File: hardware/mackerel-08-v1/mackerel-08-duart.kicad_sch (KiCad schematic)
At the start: 18 parts, among them J2 Conn_01x06, J3 Conn_01x06, J5 Conn_02x04_Odd_Even, J6 Conn_02x04_Odd_Even, J7 Conn_02x04_Odd_Even, U15 XR68C681, X2 CXO_DIP8

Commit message: Fixed most of the problems with rev 1
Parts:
- removed J5, J6, J7: Conn_02x04_Odd_Even, Connector_IDC:IDC-Header_2x04_P2.54mm_Vertical, symbol Connector_Generic:Conn_02x04_Odd_Even
- removed X2: CXO_DIP8, Oscillator:Oscillator_DIP-8, symbol Oscillator:CXO_DIP8
- added J8: Conn_01x08, Connector_PinSocket_2.54mm:PinSocket_1x08_P2.54mm_Vertical, symbol Connector_Generic:Conn_01x08
- added X2: CXO_DIP14, Oscillator:Oscillator_DIP-14, symbol Oscillator:CXO_DIP14
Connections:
- net +5V: now also X2.14 (Vcc)
- net GND: now also X2.7 (GND)
- net USR_LED: now reaches R13.1, U15.17 (OP7)
- net at U15.36 (X1/CLK): now also X2.8 (OUT)
- net SPI_CS0 renamed SPI_CS
- net SPI_CS1 renamed SD_CS
- net SPI_CS2 renamed X_OUT
- net SPI_INT0 renamed SPI_INT
- net SPI_INT1 renamed SD_CD
- no-connect marks 5 -> 4
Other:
- note added: "SD Header"
- note added: "TODO: SD card pinout"
- note removed: "No int on SPI2"
- note removed: "SPI Headers"

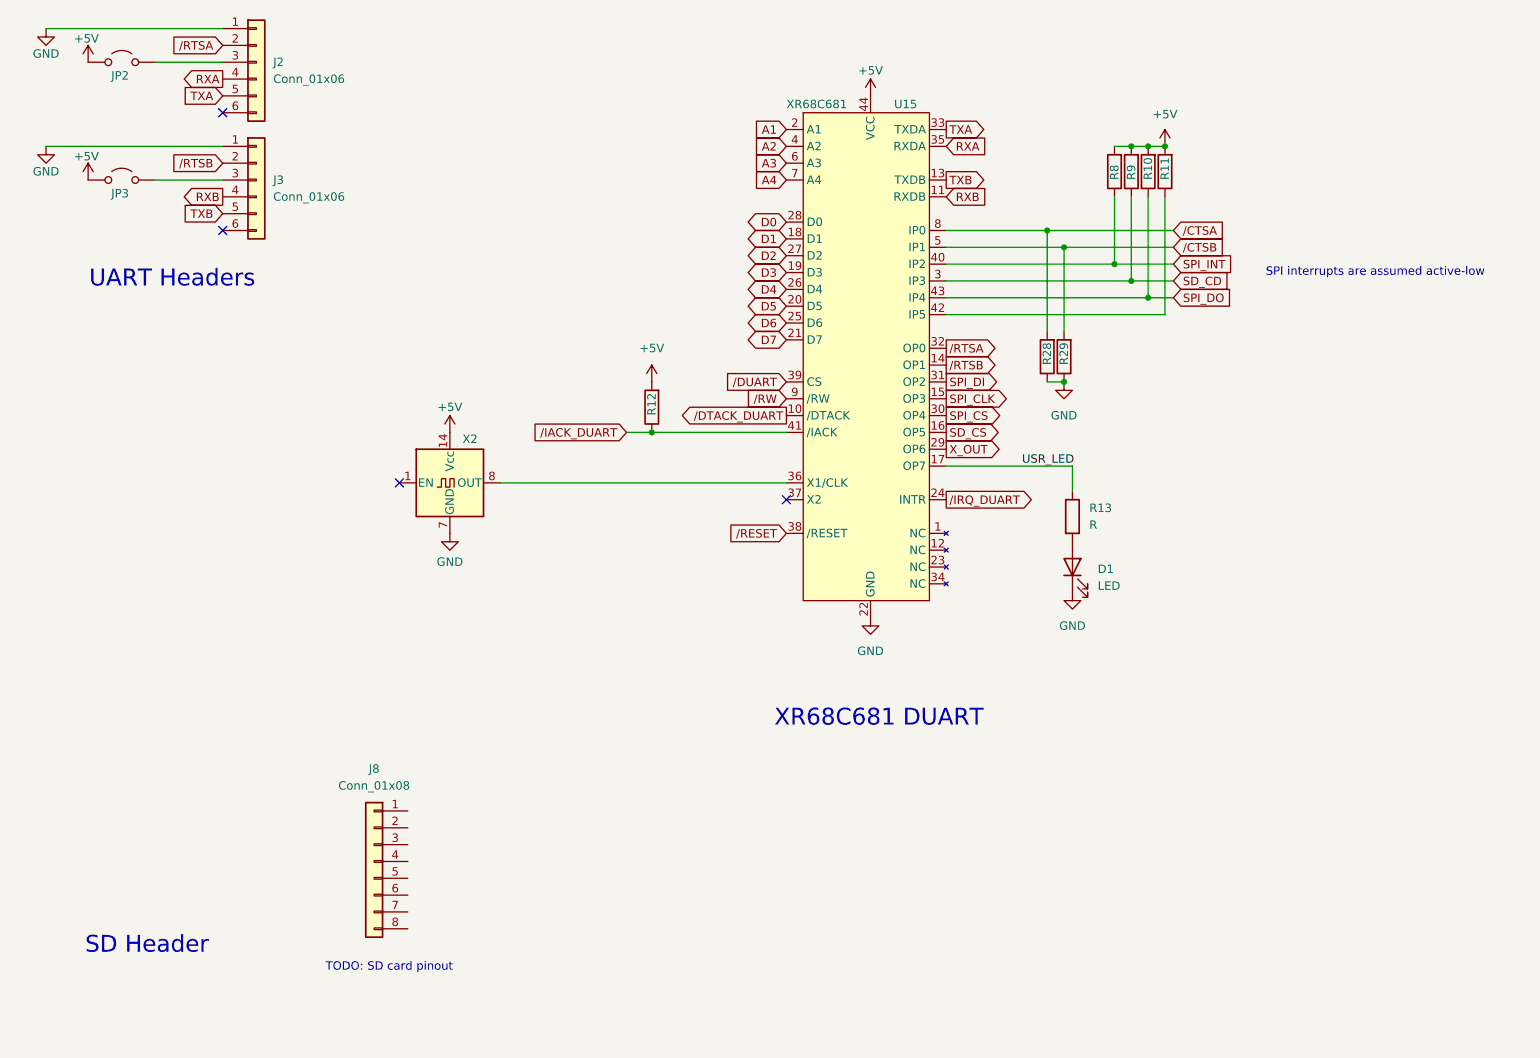
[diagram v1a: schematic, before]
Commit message: Mack-08 1.1 schematic fixes done, needs final routing
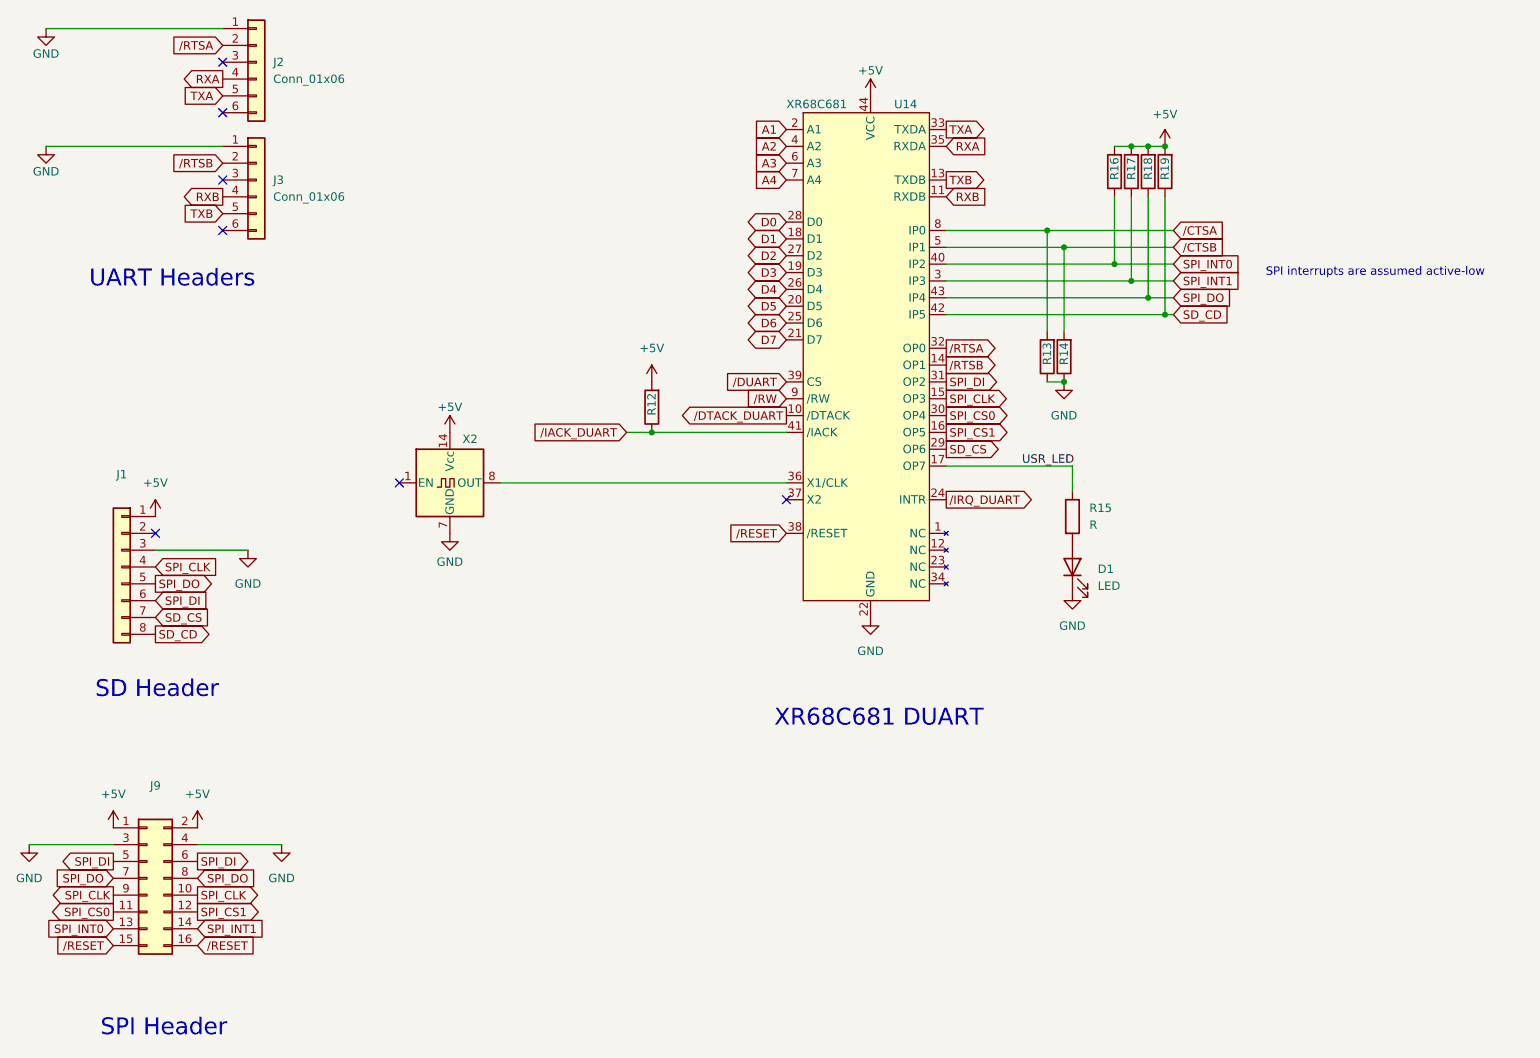
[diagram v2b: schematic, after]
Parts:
- removed J8: Conn_01x08, Connector_PinSocket_2.54mm:PinSocket_1x08_P2.54mm_Vertical, symbol Connector_Generic:Conn_01x08
- removed JP2, JP3: Jumper_2_Open, Connector_PinHeader_2.54mm:PinHeader_1x02_P2.54mm_Vertical, symbol Jumper:Jumper_2_Open
- added J1: Conn_01x08, Connector_PinSocket_2.54mm:PinSocket_1x08_P2.54mm_Vertical, symbol Connector_Generic:Conn_01x08
- added J9: Conn_02x08_Odd_Even, Connector_PinHeader_2.54mm:PinHeader_2x08_P2.54mm_Vertical, symbol Connector_Generic:Conn_02x08_Odd_Even
- renumbered R28 to R13, R29 to R14, R13 to R15, R8 to R16, R9 to R17, R10 to R18, R11 to R19, U15 to U14
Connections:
- net X_OUT is gone; now on net SD_CS: U14.29 (OP6)
- net +5V: now also J1.1 (Pin_1), J9.1 (Pin_1), J9.2 (Pin_2)
- net GND: now also J1.3 (Pin_3), J9.3 (Pin_3), J9.4 (Pin_4)
- net SD_CD: now also R19.1, U14.42 (IP5), J1.8 (Pin_8); no longer R17.1, U14.3 (IP3)
- net SD_CS: now also J1.7 (Pin_7); no longer U14.16 (OP5)
- net SPI_CLK: now also J1.4 (Pin_4), J9.10 (Pin_10), J9.9 (Pin_9)
- net SPI_DI: now also J1.6 (Pin_6), J9.5 (Pin_5), J9.6 (Pin_6)
- net SPI_DO: now also J1.5 (Pin_5), J9.7 (Pin_7), J9.8 (Pin_8)
- net /RESET: now also J9.15 (Pin_15), J9.16 (Pin_16)
- net SPI_CS renamed SPI_CS0
- net SPI_CS0: now also J9.11 (Pin_11)
- net SPI_INT renamed SPI_INT0
- net SPI_INT0: now also J9.13 (Pin_13)
- new net SPI_CS1: J9.12 (Pin_12), U14.16 (OP5)
- new net SPI_INT1: J9.14 (Pin_14), R17.1, U14.3 (IP3)
- no-connect marks 4 -> 7
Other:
- note added: "SPI Header"
- note removed: "TODO: SD card pinout"

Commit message: Mack-08 rev 1.1 routed
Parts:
- R12, R13, R14, R15, R16, R17, R18, R19: footprint Resistor_THT:R_Axial_DIN0207_L6.3mm_D2.5mm_P7.62mm_Horizontal -> Resistor_SMD:R_1206_3216Metric_Pad1.30x1.75mm_HandSolder
- renumbered J9 to J2, J2 to J3, J3 to J4
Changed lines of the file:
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@@
 			)
 		)
-		(property "Footprint" "Resistor_THT:R_Axial_DIN0207_L6.3mm_D2.5mm_P7.62mm_Horizontal"
+		(property "Footprint" "Resistor_SMD:R_1206_3216Metric_Pad1.30x1.75mm_HandSolder"
 			(at 119.888 80.01 90)
 			(effects
@@
 		(dnp no)
 		(fields_autoplaced yes)
-		(property "Reference" "#PWR044"
+		(property "Reference" "#PWR046"
 			(at 151.13 118.11 0)
 			(effects
@@
 			(project "mackerel-08-v1"
 				(path "/d8b1bce0-db11-4fa6-8e54-fcae9a8fcfc2/377dc58c-bf3b-4b5b-9c36-5a4dfaf86cf7"
-					(reference "#PWR044")
+					(reference "#PWR046")
 					(unit 1)
 				)
@@
 		(dnp no)
 		(fields_autoplaced yes)
-		(property "Reference" "#PWR045"
+		(property "Reference" "#PWR047"
 			(at 180.34 82.55 0)
 			(effects
@@
 			(project ""
 				(path "/d8b1bce0-db11-4fa6-8e54-fcae9a8fcfc2/377dc58c-bf3b-4b5b-9c36-5a4dfaf86cf7"
-					(reference "#PWR045")
+					(reference "#PWR047")
 					(unit 1)
 				)
@@
 			)
 		)
-		(property "Footprint" "Resistor_THT:R_Axial_DIN0207_L6.3mm_D2.5mm_P7.62mm_Horizontal"
+		(property "Footprint" "Resistor_SMD:R_1206_3216Metric_Pad1.30x1.75mm_HandSolder"
 			(at 192.278 44.45 90)
 			(effects
@@
 		(dnp no)
 		(fields_autoplaced yes)
-		(property "Reference" "#PWR075"
+		(property "Reference" "#PWR034"
 			(at 24.13 152.4 0)
 			(effects
@@
 			(project "mackerel-08-v1"
 				(path "/d8b1bce0-db11-4fa6-8e54-fcae9a8fcfc2/377dc58c-bf3b-4b5b-9c36-5a4dfaf86cf7"
-					(reference "#PWR075")
+					(reference "#PWR034")
 					(unit 1)
 				)
@@
 			)
 		)
-		(property "Footprint" "Resistor_THT:R_Axial_DIN0207_L6.3mm_D2.5mm_P7.62mm_Horizontal"
+		(property "Footprint" "Resistor_SMD:R_1206_3216Metric_Pad1.30x1.75mm_HandSolder"
 			(at 194.818 44.45 90)
 			(effects
@@
 		(dnp no)
 		(fields_autoplaced yes)
-		(property "Reference" "J3"
+		(property "Reference" "J4"
 			(at 60.96 45.7199 0)
 			(effects
@@
 			(project "mackerel-08-v1"
 				(path "/d8b1bce0-db11-4fa6-8e54-fcae9a8fcfc2/377dc58c-bf3b-4b5b-9c36-5a4dfaf86cf7"
-					(reference "J3")
+					(reference "J4")
 					(unit 1)
 				)
@@
 		(on_board yes)
 		(dnp no)
-		(property "Reference" "#PWR043"
+		(property "Reference" "#PWR045"
 			(at 151.13 36.83 0)
 			(effects
@@
 			(project "mackerel-08-v1"
 				(path "/d8b1bce0-db11-4fa6-8e54-fcae9a8fcfc2/377dc58c-bf3b-4b5b-9c36-5a4dfaf86cf7"
-					(reference "#PWR043")
+					(reference "#PWR045")
 					(unit 1)
 				)
@@
 		(dnp no)
 		(fields_autoplaced yes)
-		(property "Reference" "J9"
+		(property "Reference" "J2"
 			(at 43.18 137.16 0)
 			(effects
@@
 			(project ""
 				(path "/d8b1bce0-db11-4fa6-8e54-fcae9a8fcfc2/377dc58c-bf3b-4b5b-9c36-5a4dfaf86cf7"
-					(reference "J9")
+					(reference "J2")
 					(unit 1)
 				)
@@
 		(dnp no)
 		(fields_autoplaced yes)
-		(property "Reference" "#PWR046"
+		(property "Reference" "#PWR048"
 			(at 181.61 114.3 0)
 			(effects
@@
 			(project "mackerel-08-v1"
 				(path "/d8b1bce0-db11-4fa6-8e54-fcae9a8fcfc2/377dc58c-bf3b-4b5b-9c36-5a4dfaf86cf7"
-					(reference "#PWR046")
+					(reference "#PWR048")
 					(unit 1)
 				)
@@
 			)
 		)
-		(property "Footprint" "Resistor_THT:R_Axial_DIN0207_L6.3mm_D2.5mm_P7.62mm_Horizontal"
+		(property "Footprint" "Resistor_SMD:R_1206_3216Metric_Pad1.30x1.75mm_HandSolder"
 			(at 179.578 72.39 90)
 			(effects
@@
 		(dnp no)
 		(fields_autoplaced yes)
-		(property "Reference" "#PWR076"
+		(property "Reference" "#PWR041"
 			(at 62.23 152.4 0)
 			(effects
@@
 			(project "mackerel-08-v1"
 				(path "/d8b1bce0-db11-4fa6-8e54-fcae9a8fcfc2/377dc58c-bf3b-4b5b-9c36-5a4dfaf86cf7"
-					(reference "#PWR076")
+					(reference "#PWR041")
 					(unit 1)
 				)
@@
 		(on_board yes)
 		(dnp no)
-		(property "Reference" "#PWR041"
+		(property "Reference" "#PWR043"
 			(at 87.63 105.41 0)
 			(effects
@@
 			(project "mackerel-08-v1"
 				(path "/d8b1bce0-db11-4fa6-8e54-fcae9a8fcfc2/377dc58c-bf3b-4b5b-9c36-5a4dfaf86cf7"
-					(reference "#PWR041")
+					(reference "#PWR043")
 					(unit 1)
 				)
@@
 			)
 		)
-		(property "Footprint" "Resistor_THT:R_Axial_DIN0207_L6.3mm_D2.5mm_P7.62mm_Horizontal"
+		(property "Footprint" "Resistor_SMD:R_1206_3216Metric_Pad1.30x1.75mm_HandSolder"
 			(at 182.118 72.39 90)
 			(effects
@@
 		(on_board yes)
 		(dnp no)
-		(property "Reference" "#PWR035"
+		(property "Reference" "#PWR036"
 			(at 26.67 46.99 0)
 			(effects
@@
 			(project "mackerel-08-v1"
 				(path "/d8b1bce0-db11-4fa6-8e54-fcae9a8fcfc2/377dc58c-bf3b-4b5b-9c36-5a4dfaf86cf7"
-					(reference "#PWR035")
+					(reference "#PWR036")
 					(unit 1)
 				)
@@
 			)
 		)
-		(property "Footprint" "Resistor_THT:R_Axial_DIN0207_L6.3mm_D2.5mm_P7.62mm_Horizontal"
+		(property "Footprint" "Resistor_SMD:R_1206_3216Metric_Pad1.30x1.75mm_HandSolder"
 			(at 197.358 44.45 90)
 			(effects
@@
 			)
 		)
-		(property "Footprint" "Resistor_THT:R_Axial_DIN0207_L6.3mm_D2.5mm_P7.62mm_Horizontal"
+		(property "Footprint" "Resistor_SMD:R_1206_3216Metric_Pad1.30x1.75mm_HandSolder"
 			(at 189.738 44.45 90)
 			(effects
@@
 		(on_board yes)
 		(dnp no)
-		(property "Reference" "#PWR040"
+		(property "Reference" "#PWR042"
 			(at 87.63 87.63 0)
 			(effects
@@
 			(project "mackerel-08-v1"
 				(path "/d8b1bce0-db11-4fa6-8e54-fcae9a8fcfc2/377dc58c-bf3b-4b5b-9c36-5a4dfaf86cf7"
-					(reference "#PWR040")
+					(reference "#PWR042")
 					(unit 1)
 				)
@@
 		(dnp no)
 		(fields_autoplaced yes)
-		(property "Reference" "#PWR069"
+		(property "Reference" "#PWR037"
 			(at 36.83 147.32 0)
 			(effects
@@
 			(project ""
 				(path "/d8b1bce0-db11-4fa6-8e54-fcae9a8fcfc2/377dc58c-bf3b-4b5b-9c36-5a4dfaf86cf7"
-					(reference "#PWR069")
+					(reference "#PWR037")
 					(unit 1)
 				)
@@
 			)
 		)
-		(property "Footprint" "Resistor_THT:R_Axial_DIN0207_L6.3mm_D2.5mm_P7.62mm_Horizontal"
+		(property "Footprint" "Resistor_SMD:R_1206_3216Metric_Pad1.30x1.75mm_HandSolder"
 			(at 179.832 96.52 90)
 			(effects
@@
 		(dnp no)
 		(fields_autoplaced yes)
-		(property "Reference" "#PWR039"
+		(property "Reference" "#PWR040"
 			(at 57.15 107.95 0)
 			(effects
@@
 			(project "mackerel-08-v1"
 				(path "/d8b1bce0-db11-4fa6-8e54-fcae9a8fcfc2/377dc58c-bf3b-4b5b-9c36-5a4dfaf86cf7"
-					(reference "#PWR039")
+					(reference "#PWR040")
 					(unit 1)
 				)
@@
 		(dnp no)
 		(fields_autoplaced yes)
-		(property "Reference" "#PWR047"
+		(property "Reference" "#PWR049"
 			(at 195.58 44.45 0)
 			(effects
@@
 			(project "mackerel-08-v1"
 				(path "/d8b1bce0-db11-4fa6-8e54-fcae9a8fcfc2/377dc58c-bf3b-4b5b-9c36-5a4dfaf86cf7"
-					(reference "#PWR047")
+					(reference "#PWR049")
 					(unit 1)
 				)
@@
 		(dnp no)
 		(fields_autoplaced yes)
-		(property "Reference" "#PWR042"
+		(property "Reference" "#PWR044"
 			(at 118.11 80.01 0)
 			(effects
@@
 			(project "mackerel-08-v1"
 				(path "/d8b1bce0-db11-4fa6-8e54-fcae9a8fcfc2/377dc58c-bf3b-4b5b-9c36-5a4dfaf86cf7"
-					(reference "#PWR042")
+					(reference "#PWR044")
 					(unit 1)
 				)
@@
 		(dnp no)
 		(fields_autoplaced yes)
-		(property "Reference" "J2"
+		(property "Reference" "J3"
 			(at 60.96 27.9399 0)
 			(effects
@@
 			(project ""
 				(path "/d8b1bce0-db11-4fa6-8e54-fcae9a8fcfc2/377dc58c-bf3b-4b5b-9c36-5a4dfaf86cf7"
-					(reference "J2")
+					(reference "J3")
 					(unit 1)
 				)
@@
 		(dnp no)
 		(fields_autoplaced yes)
-		(property "Reference" "#PWR070"
+		(property "Reference" "#PWR039"
 			(at 49.53 147.32 0)
 			(effects
@@
 			(project "mackerel-08-v1"
 				(path "/d8b1bce0-db11-4fa6-8e54-fcae9a8fcfc2/377dc58c-bf3b-4b5b-9c36-5a4dfaf86cf7"
-					(reference "#PWR070")
+					(reference "#PWR039")
 					(unit 1)
 				)
@@
 		(on_board yes)
 		(dnp no)
-		(property "Reference" "#PWR034"
+		(property "Reference" "#PWR035"
 			(at 26.67 29.21 0)
 			(effects
@@
 			(project ""
 				(path "/d8b1bce0-db11-4fa6-8e54-fcae9a8fcfc2/377dc58c-bf3b-4b5b-9c36-5a4dfaf86cf7"
-					(reference "#PWR034")
-					(unit 1)
-				)
+					(reference "#PWR035")
+					(unit 1)
+				)

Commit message: Mackerel-08 v1.1 release
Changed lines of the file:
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@@
 	(wire
 		(pts
-			(xy 26.67 40.64) (xy 53.34 40.64)
+			(xy 40.64 40.64) (xy 53.34 40.64)
 		)
 		(stroke
@@
 	(wire
 		(pts
-			(xy 26.67 22.86) (xy 53.34 22.86)
+			(xy 40.64 22.86) (xy 53.34 22.86)
 		)
 		(stroke
@@
 	(symbol
 		(lib_id "power:GND")
-		(at 26.67 40.64 0)
+		(at 40.64 40.64 0)
 		(unit 1)
 		(exclude_from_sim no)
@@
 		(dnp no)
 		(property "Reference" "#PWR036"
-			(at 26.67 46.99 0)
+			(at 40.64 46.99 0)
 			(effects
 				(font
@@
 		)
 		(property "Value" "GND"
-			(at 26.67 44.45 0)
+			(at 40.64 44.45 0)
 			(effects
 				(font
@@
 		)
 		(property "Footprint" ""
-			(at 26.67 40.64 0)
+			(at 40.64 40.64 0)
 			(effects
 				(font
@@
 		)
 		(property "Datasheet" ""
-			(at 26.67 40.64 0)
+			(at 40.64 40.64 0)
 			(effects
 				(font
@@
 		)
 		(property "Description" "Power symbol creates a global label with name \"GND\" , ground"
-			(at 26.67 40.64 0)
+			(at 40.64 40.64 0)
 			(effects
 				(font
@@
 	(symbol
 		(lib_id "power:GND")
-		(at 26.67 22.86 0)
+		(at 40.64 22.86 0)
 		(unit 1)
 		(exclude_from_sim no)
@@
 		(dnp no)
 		(property "Reference" "#PWR035"
-			(at 26.67 29.21 0)
+			(at 40.64 29.21 0)
 			(effects
 				(font
@@
 		)
 		(property "Value" "GND"
-			(at 26.67 26.67 0)
+			(at 40.64 26.67 0)
 			(effects
 				(font
@@
 		)
 		(property "Footprint" ""
-			(at 26.67 22.86 0)
+			(at 40.64 22.86 0)
 			(effects
 				(font
@@
 		)
 		(property "Datasheet" ""
-			(at 26.67 22.86 0)
+			(at 40.64 22.86 0)
 			(effects
 				(font
@@
 		)
 		(property "Description" "Power symbol creates a global label with name \"GND\" , ground"
-			(at 26.67 22.86 0)
+			(at 40.64 22.86 0)
 			(effects
 				(font

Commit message: Mackerel-08 rev 1.1 release
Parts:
- removed J2: Conn_02x08_Odd_Even, Connector_PinHeader_2.54mm:PinHeader_2x08_P2.54mm_Vertical, symbol Connector_Generic:Conn_02x08_Odd_Even
- added J2: Conn_02x09_Odd_Even, Connector_PinHeader_2.54mm:PinHeader_2x09_P2.54mm_Vertical, symbol Connector_Generic:Conn_02x09_Odd_Even
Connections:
- net +5V: now also J2.1 (Pin_1), J2.2 (Pin_2)
- net GND: now also J2.5 (Pin_5), J2.6 (Pin_6)
- net SPI_CLK: now also J2.11 (Pin_11), J2.12 (Pin_12)
- net SPI_CS0: now also J2.13 (Pin_13)
- net SPI_CS1: now also J2.14 (Pin_14)
- net SPI_DI: now also J2.7 (Pin_7), J2.8 (Pin_8)
- net SPI_DO: now also J2.10 (Pin_10), J2.9 (Pin_9)
- net SPI_INT0: now also J2.15 (Pin_15)
- net SPI_INT1: now also J2.16 (Pin_16)
- net /RESET: now also J2.17 (Pin_17), J2.18 (Pin_18)
- new net +3.3V: J2.3 (Pin_3), J2.4 (Pin_4)
